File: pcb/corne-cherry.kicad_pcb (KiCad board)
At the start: 2 copper layers, 275.5 x 105.6 mm, 190 parts, among them J1 MJ-4PP-9, J2 OLED, J3 MJ-4PP-9, J4 OLED, J5 Conn_01x01_Male, J6 Conn_01x01_Male, P1 Conn_01x03, P3 Conn_01x03, SW1 SW_PUSH, SW10 SW_PUSH, SW11 SW_PUSH, SW12 SW_PUSH, SW13 SW_PUSH, SW14 SW_PUSH, SW15 SW_PUSH, SW16 SW_PUSH, SW17 SW_PUSH, SW18 SW_PUSH, SW19 SW_PUSH, SW2 SW_PUSH, SW20 SW_PUSH, SW21 SW_PUSH, SW22 SW_PUSH, SW23 SW_PUSH, SW24 SW_PUSH, SW25 SW_PUSH, SW26 SW_PUSH, SW27 SW_PUSH, SW28 SW_PUSH, SW29 SW_PUSH, SW3 SW_PUSH, SW30 SW_PUSH, SW31 SW_PUSH, SW32 SW_PUSH, SW33 SW_PUSH, SW34 SW_PUSH, SW35 SW_PUSH, SW36 SW_PUSH, SW37 SW_PUSH, SW38 SW_PUSH, SW39 SW_PUSH, SW4 SW_PUSH, SW40 SW_PUSH, SW41 SW_PUSH, SW42 SW_PUSH, SW5 SW_PUSH, SW6 SW_PUSH, SW7 SW_PUSH, SW8 SW_PUSH, SW9 SW_PUSH, U1 ProMicro, U2 ProMicro

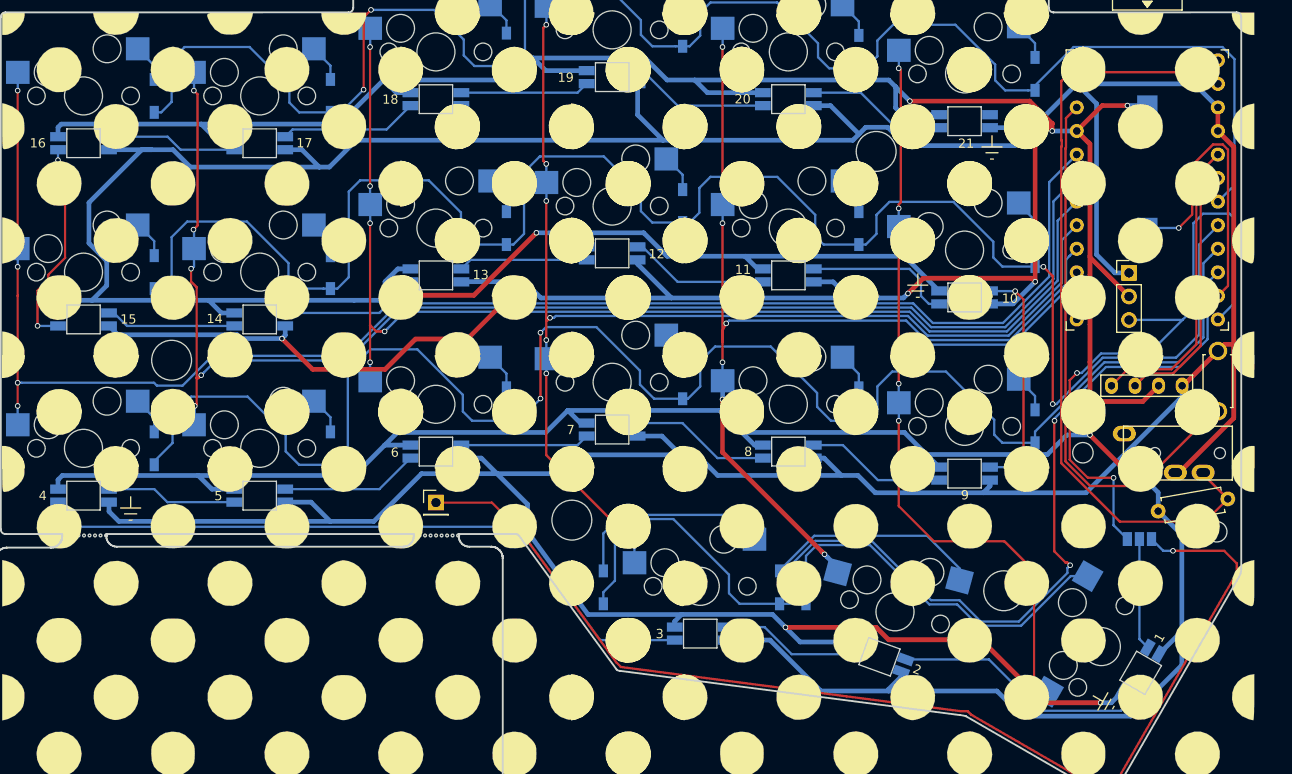
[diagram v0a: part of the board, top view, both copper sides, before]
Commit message: Start reworking PCB
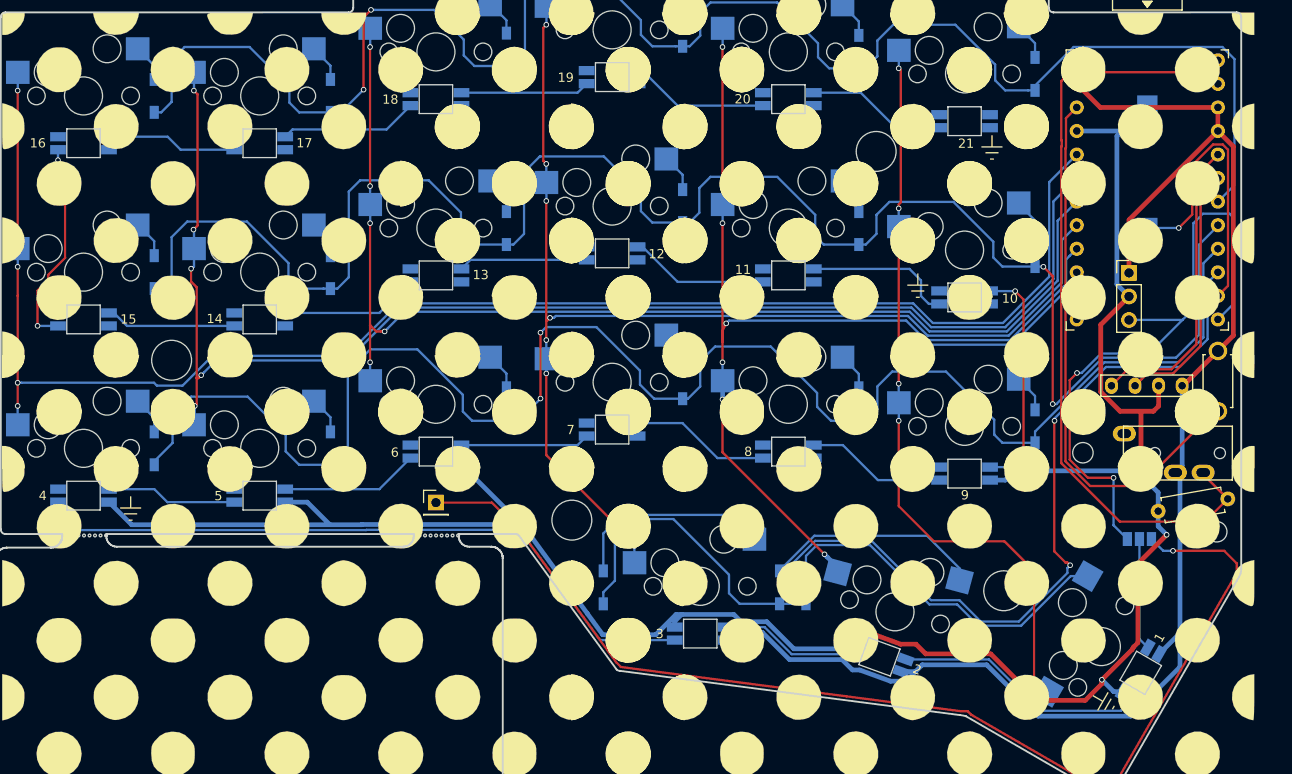
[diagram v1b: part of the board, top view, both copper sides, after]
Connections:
- LED1 pad 1: GND -> VCC
- LED1 pad 3: VCC -> GND
- LED10 pad 1: GND -> VCC
- LED10 pad 3: VCC -> GND
- LED11 pad 1: GND -> VCC
- LED11 pad 3: VCC -> GND
- LED12 pad 1: GND -> VCC
- LED12 pad 3: VCC -> GND
- LED13 pad 1: GND -> VCC
- LED13 pad 3: VCC -> GND
- LED14 pad 1: GND -> VCC
- LED14 pad 3: VCC -> GND
- LED15 pad 1: GND -> VCC
- LED15 pad 3: VCC -> GND
- LED16 pad 1: GND -> VCC
- LED16 pad 3: VCC -> GND
- LED17 pad 1: GND -> VCC
- LED17 pad 3: VCC -> GND
- LED18 pad 1: GND -> VCC
- LED18 pad 3: VCC -> GND
- LED19 pad 1: GND -> VCC
- LED19 pad 3: VCC -> GND
- LED2 pad 1: GND -> VCC
- LED2 pad 3: VCC -> GND
- LED20 pad 1: GND -> VCC
- LED20 pad 3: VCC -> GND
- LED21 pad 1: GND -> VCC
- LED21 pad 3: VCC -> GND
- LED22 pad 1: GNDA -> VDD
- LED22 pad 3: VDD -> GNDA
- LED23 pad 1: GNDA -> VDD
- LED23 pad 3: VDD -> GNDA
- LED24 pad 1: GNDA -> VDD
- LED24 pad 3: VDD -> GNDA
- LED25 pad 1: GNDA -> VDD
- LED25 pad 3: VDD -> GNDA
- LED26 pad 1: GNDA -> VDD
- LED26 pad 3: VDD -> GNDA
- LED27 pad 1: GNDA -> VDD
- LED27 pad 3: VDD -> GNDA
- LED28 pad 1: GNDA -> VDD
- LED28 pad 3: VDD -> GNDA
- LED29 pad 1: GNDA -> VDD
- LED29 pad 3: VDD -> GNDA
- LED3 pad 1: GND -> VCC
- LED3 pad 3: VCC -> GND
- LED30 pad 1: GNDA -> VDD
- LED30 pad 3: VDD -> GNDA
- LED31 pad 1: GNDA -> VDD
- LED31 pad 3: VDD -> GNDA
- LED32 pad 1: GNDA -> VDD
- LED32 pad 3: VDD -> GNDA
- LED33 pad 1: GNDA -> VDD
- LED33 pad 3: VDD -> GNDA
- LED34 pad 1: GNDA -> VDD
- LED34 pad 3: VDD -> GNDA
- LED35 pad 1: GNDA -> VDD
- LED35 pad 3: VDD -> GNDA
- LED36 pad 1: GNDA -> VDD
- LED36 pad 3: VDD -> GNDA
- LED37 pad 1: GNDA -> VDD
- LED37 pad 3: VDD -> GNDA
- LED38 pad 1: GNDA -> VDD
- LED38 pad 3: VDD -> GNDA
- LED39 pad 1: GNDA -> VDD
- LED39 pad 3: VDD -> GNDA
- LED4 pad 1: GND -> VCC
- LED4 pad 3: VCC -> GND
- LED40 pad 1: GNDA -> VDD
- LED40 pad 3: VDD -> GNDA
- LED41 pad 1: GNDA -> VDD
- LED41 pad 3: VDD -> GNDA
- LED42 pad 1: GNDA -> VDD
- LED42 pad 3: VDD -> GNDA
- LED5 pad 1: GND -> VCC
- LED5 pad 3: VCC -> GND
- LED6 pad 1: GND -> VCC
- LED6 pad 3: VCC -> GND
- LED7 pad 1: GND -> VCC
- LED7 pad 3: VCC -> GND
- LED8 pad 1: GND -> VCC
- LED8 pad 3: VCC -> GND
- LED9 pad 1: GND -> VCC
- LED9 pad 3: VCC -> GND
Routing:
- net GND: track 603.1 -> 160.6 mm, vias 4 -> 0
- net VCC: track 577.5 -> 239.8 mm, vias 8 -> 3

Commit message: Update more RGB stuff
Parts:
- moved D9 0.76 mm to (66.2, 49.4)
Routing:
- net GNDA: track 601.4 -> 91.3 mm, vias 6 -> 0
- net GND: track 160.6 -> 557.8 mm, vias 0 -> 6
- net VDD: track 576.6 -> 190.3 mm, vias 8 -> 0
- net VCC: track 239.8 -> 511.5 mm, vias 3 -> 5
- net Net-(LED15-Pad4): track 16.6 -> 15.6 mm
- net row1: track 193.3 -> 192.4 mm

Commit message: Almost done with RGB
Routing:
- net GNDA: track 91.3 -> 538.5 mm, vias 0 -> 5
- net VDD: track 190.3 -> 456.8 mm
- net row2_r: track 172.6 -> 164.2 mm, vias 2 -> 4
- net Net-(LED41-Pad4): track 22.3 -> 29.2 mm, vias 2 -> 0

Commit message: Finish RGB
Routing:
- net VDD: track 456.8 -> 525.7 mm
- net row1_r: track 166.9 -> 164.8 mm, vias 0 -> 2
- net GNDA: track 538.5 -> 539.1 mm

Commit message: Add encoder to left half
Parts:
- removed the G*** at (91.1, 32.9)
- removed the G*** at (109.5, 88.3)
- removed the G*** at (48.2, 88.3)
- removed the G*** at (207.3, 32.8)
- removed the G*** at (250.2, 88.1)
- removed the G*** at (188.9, 88.1)
- removed the G*** at (250.2, 51.3)
- removed the G*** at (188.9, 51.3)
- removed the G*** at (109.5, 51.3)
- removed the G*** at (48.2, 51.3)
- added SW43: Rotary_Encoder_Switch, Keebio-Parts:RotaryEncoder_EC11-no-legs, F.Cu at (20.1, 36.1)
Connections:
- SW1 pad 1: Net-(SW1-Pad1) -> col0
- U1 pad 13: Net-(U1-Pad13) -> ENC_B
- U1 pad 14: Net-(U1-Pad14) -> ENC_A
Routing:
- net ENC_B: track 0.00 -> 141.2 mm, vias 0 -> 2
- net ENC_A: track 0.00 -> 140.1 mm, vias 0 -> 1
- net GND: track 557.8 -> 574.0 mm
- net col0: track 170.3 -> 177.9 mm
- net Net-(D1-Pad2): track 4.04 -> 8.14 mm
- net Net-(LED1-Pad4): track 22.7 -> 25.4 mm
- net VDD: track 525.7 -> 527.6 mm
- net (no net): track 0.00 -> 1.55 mm
- net VCC: track 511.5 -> 512.9 mm
- net Net-(JP2-Pad2): track 75.4 -> 76.6 mm

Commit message: Finish PCB
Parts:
- added G***: LOGO, svg:ae1, B.Cu at (160.9, 43.5)
- added SW44: Rotary_Encoder_Switch, Keebio-Parts:RotaryEncoder_EC11-no-legs, F.Cu at (276.6, 36.1)
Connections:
- SW22 pad 1: Net-(SW22-Pad1) -> col0_r
- U2 pad 13: Net-(U2-Pad13) -> ENC_B_R
- U2 pad 14: Net-(U2-Pad14) -> ENC_A_R
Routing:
- net ENC_A_R: track 0.00 -> 257.1 mm, vias 0 -> 5
- net ENC_B_R: track 0.00 -> 160.4 mm, vias 0 -> 4
- net GNDA: track 539.1 -> 564.7 mm, vias 5 -> 6
- net row1_r: track 164.8 -> 153.2 mm
- net row0_r: track 184.4 -> 175.6 mm
- net VDD: track 527.6 -> 536.0 mm
- net col0_r: track 175.8 -> 183.8 mm
- net GND: track 574.0 -> 569.8 mm
- net Net-(D22-Pad2): track 4.05 -> 8.15 mm
